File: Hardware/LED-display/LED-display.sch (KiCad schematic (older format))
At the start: 117 parts, among them J1 Conn_01x08, U1 74HC595, U2 74HC595, U3 74HC595

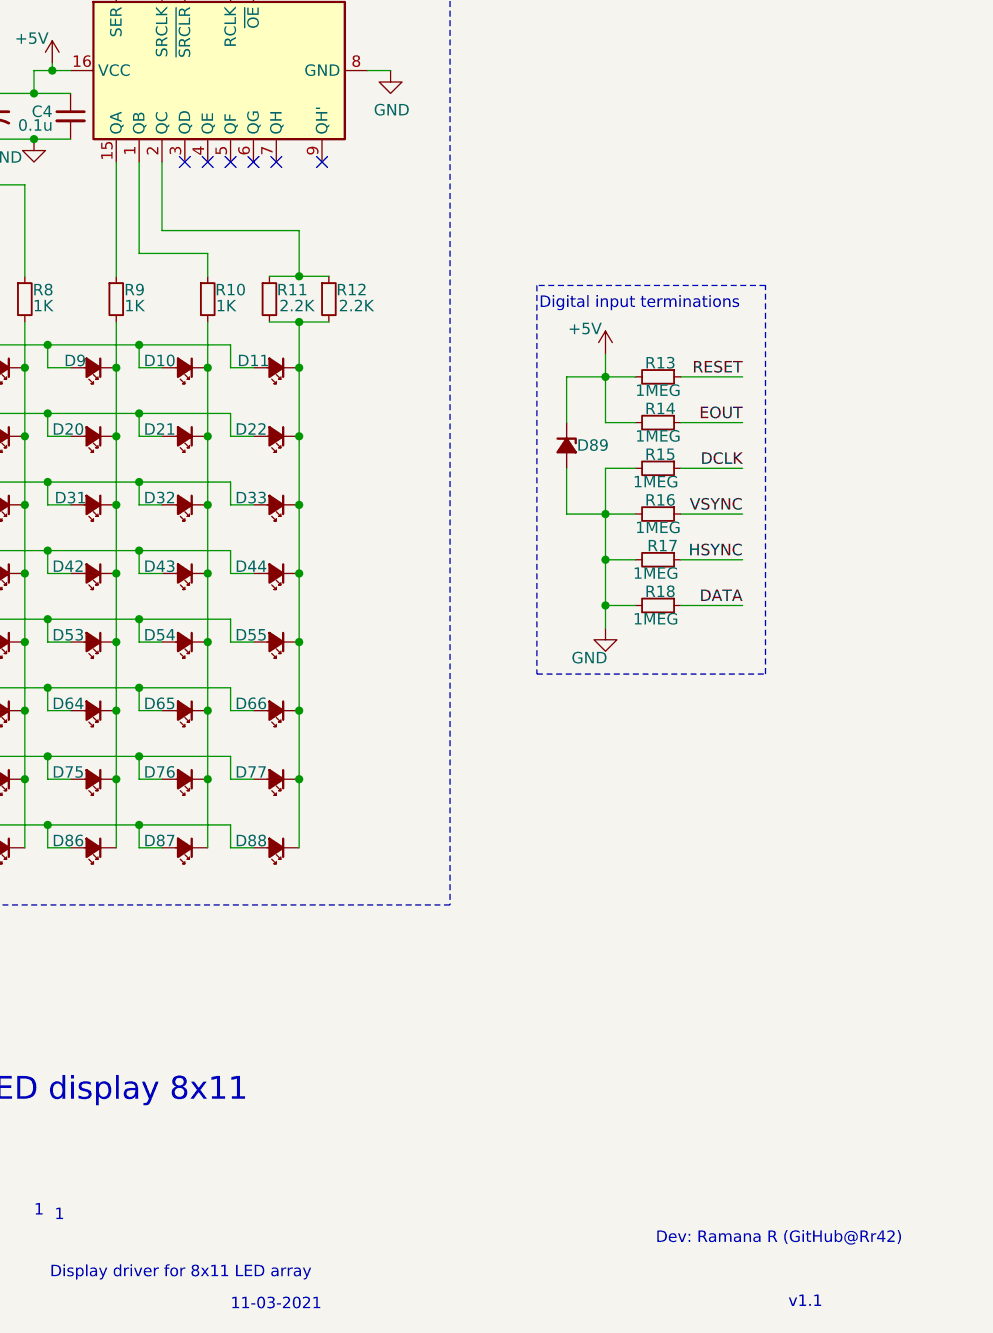
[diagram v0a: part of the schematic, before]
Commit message: Replaced parllel 2.2K resistors with 1k to match other LEDs
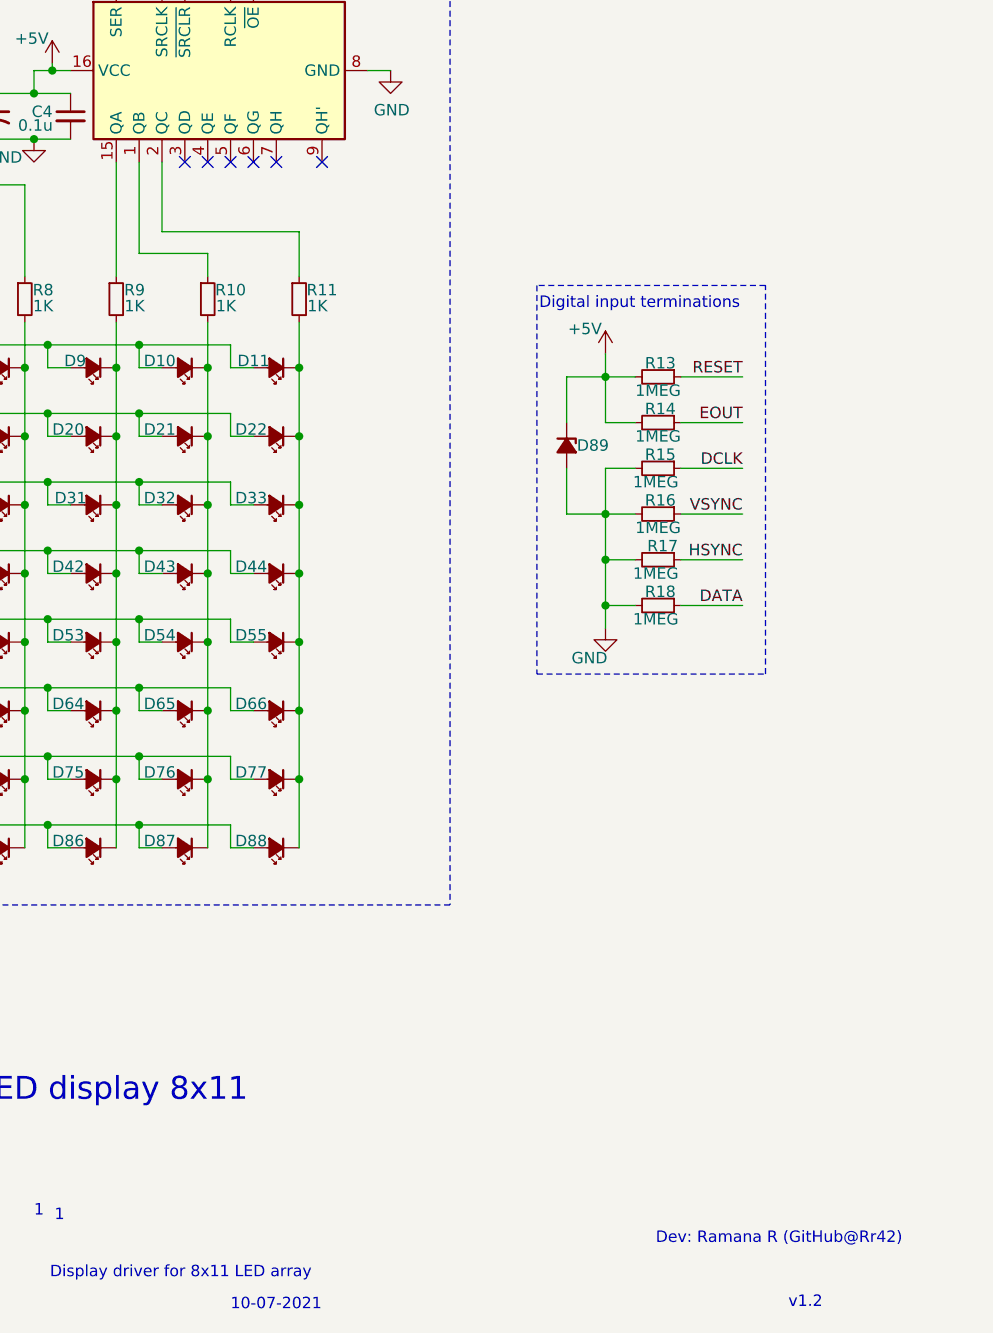
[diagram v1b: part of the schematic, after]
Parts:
- removed R12: 2.2K, Resistor_THT:R_Axial_DIN0207_L6.3mm_D2.5mm_P7.62mm_Horizontal, symbol Device:R_Small
- C1, C3, C5: footprint Capacitor_THT:CP_Radial_D4.0mm_P2.00mm -> Capacitors_THT:CP_Radial_D5.0mm_P2.00mm
- C2, C4, C6: footprint Capacitor_THT:C_Disc_D4.7mm_W2.5mm_P5.00mm -> Capacitors_THT:C_Disc_D5.1mm_W3.2mm_P5.00mm
- R1, R10, R2, R3, R4, R5, R6, R7, R8, R9: footprint Resistor_THT:R_Axial_DIN0309_L9.0mm_D3.2mm_P12.70mm_Horizontal -> Resistors_THT:R_Axial_DIN0207_L6.3mm_D2.5mm_P7.62mm_Horizontal
- R11: value 2.2K -> 1K; footprint Resistor_THT:R_Axial_DIN0207_L6.3mm_D2.5mm_P7.62mm_Horizontal -> Resistors_THT:R_Axial_DIN0207_L6.3mm_D2.5mm_P7.62mm_Horizontal
- R13, R14, R15, R16, R17, R18: footprint Resistor_THT:R_Axial_DIN0207_L6.3mm_D2.5mm_P7.62mm_Horizontal -> Resistors_THT:R_Axial_DIN0207_L6.3mm_D2.5mm_P7.62mm_Horizontal
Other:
- note added: "10-07-2021"
- note added: "v1.2"
- note removed: "11-03-2021"
- note removed: "v1.1"
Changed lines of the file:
@@
 $EndDescr
 Text Notes 8150 7640 0    50   ~ 0
-11-03-2021
+10-07-2021
 Text Notes 10590 7630 0    50   ~ 0
-v1.1
+v1.2
 Text Notes 7290 7230 0    50   ~ 0
 1
@@
 F 0 "C3" H 6950 2440 50  0000 L CNN
 F 1 "1u" H 6950 2380 50  0000 L CNN
-F 2 "Capacitor_THT:CP_Radial_D4.0mm_P2.00mm" H 7120 2410 50  0001 C CNN
+F 2 "Capacitors_THT:CP_Radial_D5.0mm_P2.00mm" H 7120 2410 50  0001 C CNN
 F 3 "~" H 7120 2410 50  0001 C CNN
 	1    7120 2410
@@
 F 0 "C4" H 7280 2430 50  0000 L CNN
 F 1 "0.1u" H 7220 2370 50  0000 L CNN
-F 2 "Capacitor_THT:C_Disc_D4.7mm_W2.5mm_P5.00mm" H 7450 2410 50  0001 C CNN
+F 2 "Capacitors_THT:C_Disc_D5.1mm_W3.2mm_P5.00mm" H 7450 2410 50  0001 C CNN
 F 3 "~" H 7450 2410 50  0001 C CNN
 	1    7450 2410
@@
 F 0 "C1" H 4800 2440 50  0000 L CNN
 F 1 "1u" H 4800 2380 50  0000 L CNN
-F 2 "Capacitor_THT:CP_Radial_D4.0mm_P2.00mm" H 4970 2410 50  0001 C CNN
+F 2 "Capacitors_THT:CP_Radial_D5.0mm_P2.00mm" H 4970 2410 50  0001 C CNN
 F 3 "~" H 4970 2410 50  0001 C CNN
 	1    4970 2410
@@
 F 0 "C2" H 5130 2430 50  0000 L CNN
 F 1 "0.1u" H 5070 2370 50  0000 L CNN
-F 2 "Capacitor_THT:C_Disc_D4.7mm_W2.5mm_P5.00mm" H 5300 2410 50  0001 C CNN
+F 2 "Capacitors_THT:C_Disc_D5.1mm_W3.2mm_P5.00mm" H 5300 2410 50  0001 C CNN
 F 3 "~" H 5300 2410 50  0001 C CNN
 	1    5300 2410
@@
 F 0 "C5" H 3090 3620 50  0000 L CNN
 F 1 "1u" H 3090 3560 50  0000 L CNN
-F 2 "Capacitor_THT:CP_Radial_D4.0mm_P2.00mm" H 3260 3590 50  0001 C CNN
+F 2 "Capacitors_THT:CP_Radial_D5.0mm_P2.00mm" H 3260 3590 50  0001 C CNN
 F 3 "~" H 3260 3590 50  0001 C CNN
 	1    3260 3590
@@
 F 0 "C6" H 3420 3610 50  0000 L CNN
 F 1 "0.1u" H 3360 3550 50  0000 L CNN
-F 2 "Capacitor_THT:C_Disc_D4.7mm_W2.5mm_P5.00mm" H 3590 3590 50  0001 C CNN
+F 2 "Capacitors_THT:C_Disc_D5.1mm_W3.2mm_P5.00mm" H 3590 3590 50  0001 C CNN
 F 3 "~" H 3590 3590 50  0001 C CNN
 	1    3590 3590
@@
 	5500 2610 5500 2710
 Wire Wire Line
-	8450 2910 8450 3110
-Wire Wire Line
-	7850 2910 8450 2910
-Wire Wire Line
-	7850 2610 7850 2910
-Wire Wire Line
 	7750 3010 8050 3010
 Wire Wire Line
@@
 Wire Wire Line
 	8050 3010 8050 3110
-Wire Wire Line
-	8450 3110 8580 3110
-Connection ~ 8450 3110
-Wire Wire Line
-	8320 3110 8450 3110
 $Comp
 L power:+5V #PWR012
@@
 	4050 4310 4150 4310
 $Comp
-L Device:R_Small R12
-U 1 1 60D65C92
-P 8580 3210
-F 0 "R12" H 8680 3250 50  0000 C CNN
-F 1 "2.2K" H 8700 3180 50  0000 C CNN
-F 2 "Resistor_THT:R_Axial_DIN0207_L6.3mm_D2.5mm_P7.62mm_Horizontal" H 8580 3210 50  0001 C CNN
-F 3 "~" H 8580 3210 50  0001 C CNN
-	1    8580 3210
-	1    0    0    -1
-$EndComp
-$Comp
 L Device:R_Small R10
 U 1 1 60D4072C
@@
 F 0 "R10" H 8150 3250 50  0000 C CNN
 F 1 "1K" H 8130 3180 50  0000 C CNN
-F 2 "Resistor_THT:R_Axial_DIN0309_L9.0mm_D3.2mm_P12.70mm_Horizontal" H 8050 3210 50  0001 C CNN
+F 2 "Resistors_THT:R_Axial_DIN0207_L6.3mm_D2.5mm_P7.62mm_Horizontal" H 8050 3210 50  0001 C CNN
 F 3 "~" H 8050 3210 50  0001 C CNN
 	1    8050 3210
@@
 F 0 "R9" H 7730 3250 50  0000 C CNN
 F 1 "1K" H 7730 3180 50  0000 C CNN
-F 2 "Resistor_THT:R_Axial_DIN0309_L9.0mm_D3.2mm_P12.70mm_Horizontal" H 7650 3210 50  0001 C CNN
+F 2 "Resistors_THT:R_Axial_DIN0207_L6.3mm_D2.5mm_P7.62mm_Horizontal" H 7650 3210 50  0001 C CNN
 F 3 "~" H 7650 3210 50  0001 C CNN
 	1    7650 3210
@@
 F 0 "R8" H 7330 3250 50  0000 C CNN
 F 1 "1K" H 7330 3180 50  0000 C CNN
-F 2 "Resistor_THT:R_Axial_DIN0309_L9.0mm_D3.2mm_P12.70mm_Horizontal" H 7250 3210 50  0001 C CNN
+F 2 "Resistors_THT:R_Axial_DIN0207_L6.3mm_D2.5mm_P7.62mm_Horizontal" H 7250 3210 50  0001 C CNN
 F 3 "~" H 7250 3210 50  0001 C CNN
 	1    7250 3210
@@
 F 0 "R7" H 6930 3250 50  0000 C CNN
 F 1 "1K" H 6930 3180 50  0000 C CNN
-F 2 "Resistor_THT:R_Axial_DIN0309_L9.0mm_D3.2mm_P12.70mm_Horizontal" H 6850 3210 50  0001 C CNN
+F 2 "Resistors_THT:R_Axial_DIN0207_L6.3mm_D2.5mm_P7.62mm_Horizontal" H 6850 3210 50  0001 C CNN
 F 3 "~" H 6850 3210 50  0001 C CNN
 	1    6850 3210
@@
 F 0 "R6" H 6530 3250 50  0000 C CNN
 F 1 "1K" H 6530 3180 50  0000 C CNN
-F 2 "Resistor_THT:R_Axial_DIN0309_L9.0mm_D3.2mm_P12.70mm_Horizontal" H 6450 3210 50  0001 C CNN
+F 2 "Resistors_THT:R_Axial_DIN0207_L6.3mm_D2.5mm_P7.62mm_Horizontal" H 6450 3210 50  0001 C CNN
 F 3 "~" H 6450 3210 50  0001 C CNN
 	1    6450 3210
@@
 F 0 "R5" H 6130 3250 50  0000 C CNN
 F 1 "1K" H 6130 3180 50  0000 C CNN
-F 2 "Resistor_THT:R_Axial_DIN0309_L9.0mm_D3.2mm_P12.70mm_Horizontal" H 6050 3210 50  0001 C CNN
+F 2 "Resistors_THT:R_Axial_DIN0207_L6.3mm_D2.5mm_P7.62mm_Horizontal" H 6050 3210 50  0001 C CNN
 F 3 "~" H 6050 3210 50  0001 C CNN
 	1    6050 3210
@@
 F 0 "R4" H 5730 3250 50  0000 C CNN
 F 1 "1K" H 5730 3180 50  0000 C CNN
-F 2 "Resistor_THT:R_Axial_DIN0309_L9.0mm_D3.2mm_P12.70mm_Horizontal" H 5650 3210 50  0001 C CNN
+F 2 "Resistors_THT:R_Axial_DIN0207_L6.3mm_D2.5mm_P7.62mm_Horizontal" H 5650 3210 50  0001 C CNN
 F 3 "~" H 5650 3210 50  0001 C CNN
 	1    5650 3210
@@
 F 0 "R3" H 5330 3250 50  0000 C CNN
 F 1 "1K" H 5330 3180 50  0000 C CNN
-F 2 "Resistor_THT:R_Axial_DIN0309_L9.0mm_D3.2mm_P12.70mm_Horizontal" H 5250 3210 50  0001 C CNN
+F 2 "Resistors_THT:R_Axial_DIN0207_L6.3mm_D2.5mm_P7.62mm_Horizontal" H 5250 3210 50  0001 C CNN
 F 3 "~" H 5250 3210 50  0001 C CNN
 	1    5250 3210
@@
 F 0 "R2" H 4930 3250 50  0000 C CNN
 F 1 "1K" H 4930 3180 50  0000 C CNN
-F 2 "Resistor_THT:R_Axial_DIN0309_L9.0mm_D3.2mm_P12.70mm_Horizontal" H 4850 3210 50  0001 C CNN
+F 2 "Resistors_THT:R_Axial_DIN0207_L6.3mm_D2.5mm_P7.62mm_Horizontal" H 4850 3210 50  0001 C CNN
 F 3 "~" H 4850 3210 50  0001 C CNN
 	1    4850 3210
 	1    0    0    -1
 $EndComp
-Wire Wire Line
-	8450 3310 8580 3310
-Connection ~ 8450 3310
-Wire Wire Line
-	8320 3310 8450 3310
-$Comp
-L Device:R_Small R11
-U 1 1 60C737DB
-P 8320 3210
-F 0 "R11" H 8420 3250 50  0000 C CNN
-F 1 "2.2K" H 8440 3180 50  0000 C CNN
-F 2 "Resistor_THT:R_Axial_DIN0207_L6.3mm_D2.5mm_P7.62mm_Horizontal" H 8320 3210 50  0001 C CNN
-F 3 "~" H 8320 3210 50  0001 C CNN
-	1    8320 3210
-	1    0    0    -1
-$EndComp
 $Comp
 L Device:R_Small R1
@@
 F 0 "R1" H 4530 3250 50  0000 C CNN
 F 1 "1K" H 4530 3180 50  0000 C CNN
-F 2 "Resistor_THT:R_Axial_DIN0309_L9.0mm_D3.2mm_P12.70mm_Horizontal" H 4450 3210 50  0001 C CNN
+F 2 "Resistors_THT:R_Axial_DIN0207_L6.3mm_D2.5mm_P7.62mm_Horizontal" H 4450 3210 50  0001 C CNN
 F 3 "~" H 4450 3210 50  0001 C CNN
 	1    4450 3210
 	1    0    0    -1
 $EndComp
-Wire Wire Line
-	8450 3510 8450 3810
-Connection ~ 8450 3510
-Wire Wire Line
-	8450 3310 8450 3510
 Connection ~ 4150 4610
 Connection ~ 4150 4310
@@
 F 0 "R13" V 9960 3560 50  0000 C CNN
 F 1 "1MEG" V 10080 3550 50  0000 C CNN
-F 2 "Resistor_THT:R_Axial_DIN0207_L6.3mm_D2.5mm_P7.62mm_Horizontal" H 10020 3550 50  0001 C CNN
+F 2 "Resistors_THT:R_Axial_DIN0207_L6.3mm_D2.5mm_P7.62mm_Horizontal" H 10020 3550 50  0001 C CNN
 F 3 "~" H 10020 3550 50  0001 C CNN
 	1    10020 3550
@@
 F 0 "R14" V 9960 3760 50  0000 C CNN
 F 1 "1MEG" V 10080 3750 50  0000 C CNN
-F 2 "Resistor_THT:R_Axial_DIN0207_L6.3mm_D2.5mm_P7.62mm_Horizontal" H 10020 3750 50  0001 C CNN
+F 2 "Resistors_THT:R_Axial_DIN0207_L6.3mm_D2.5mm_P7.62mm_Horizontal" H 10020 3750 50  0001 C CNN
 F 3 "~" H 10020 3750 50  0001 C CNN
 	1    10020 3750
@@
 F 0 "R15" V 9960 3960 50  0000 C CNN
 F 1 "1MEG" V 10080 3940 50  0000 C CNN
-F 2 "Resistor_THT:R_Axial_DIN0207_L6.3mm_D2.5mm_P7.62mm_Horizontal" H 10020 3950 50  0001 C CNN
+F 2 "Resistors_THT:R_Axial_DIN0207_L6.3mm_D2.5mm_P7.62mm_Horizontal" H 10020 3950 50  0001 C CNN
 F 3 "~" H 10020 3950 50  0001 C CNN
 	1    10020 3950
@@
 F 0 "R16" V 9960 4160 50  0000 C CNN
 F 1 "1MEG" V 10080 4150 50  0000 C CNN
-F 2 "Resistor_THT:R_Axial_DIN0207_L6.3mm_D2.5mm_P7.62mm_Horizontal" H 10020 4150 50  0001 C CNN
+F 2 "Resistors_THT:R_Axial_DIN0207_L6.3mm_D2.5mm_P7.62mm_Horizontal" H 10020 4150 50  0001 C CNN
 F 3 "~" H 10020 4150 50  0001 C CNN
 	1    10020 4150
@@
 F 0 "R17" V 9960 4370 50  0000 C CNN
 F 1 "1MEG" V 10080 4340 50  0000 C CNN
-F 2 "Resistor_THT:R_Axial_DIN0207_L6.3mm_D2.5mm_P7.62mm_Horizontal" H 10020 4350 50  0001 C CNN
+F 2 "Resistors_THT:R_Axial_DIN0207_L6.3mm_D2.5mm_P7.62mm_Horizontal" H 10020 4350 50  0001 C CNN
 F 3 "~" H 10020 4350 50  0001 C CNN
 	1    10020 4350
@@
 F 0 "R18" V 9960 4560 50  0000 C CNN
 F 1 "1MEG" V 10080 4540 50  0000 C CNN
-F 2 "Resistor_THT:R_Axial_DIN0207_L6.3mm_D2.5mm_P7.62mm_Horizontal" H 10020 4550 50  0001 C CNN
+F 2 "Resistors_THT:R_Axial_DIN0207_L6.3mm_D2.5mm_P7.62mm_Horizontal" H 10020 4550 50  0001 C CNN
 F 3 "~" H 10020 4550 50  0001 C CNN
 	1    10020 4550
@@
 Text Notes 9500 3260 0    50   ~ 0
 Digital input terminations
+$Comp
+L Device:R_Small R11
+U 1 1 611590D5
+P 8450 3210
+F 0 "R11" H 8550 3250 50  0000 C CNN
+F 1 "1K" H 8530 3180 50  0000 C CNN
+F 2 "Resistors_THT:R_Axial_DIN0207_L6.3mm_D2.5mm_P7.62mm_Horizontal" H 8450 3210 50  0001 C CNN
+F 3 "~" H 8450 3210 50  0001 C CNN
+	1    8450 3210
+	1    0    0    -1
+$EndComp
+Wire Wire Line
+	8450 3510 8450 3810
+Wire Wire Line
+	8450 3510 8450 3310
+Connection ~ 8450 3510
+Wire Wire Line
+	8450 3110 8450 2915
+Wire Wire Line
+	7850 2915 7850 2610
+Wire Wire Line
+	7850 2915 8450 2915
 $EndSCHEMATC
